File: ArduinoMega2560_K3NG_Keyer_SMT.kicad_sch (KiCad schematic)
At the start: 44 parts, among them J10 Conn_01x05_Strip, J11 Conn_01x05_Strip, J12 Conn_01x05_Strip, J13 Conn_01x05_Strip, J2 Conn_01x02, J23 Conn_01x02, J25 Conn_01x05_Strip, J26 Conn_01x05_Strip, J27 Conn_01x05_Strip, J28 Conn_01x05_Strip, J29 Conn_01x05_Strip, J30 Conn_01x05_Strip, J31 Conn_01x05_Strip, J32 Conn_01x05_Strip, J33 Conn_01x05_Strip, J34 Conn_01x05_Strip, J35 Conn_01x05_Strip, J36 Conn_01x05_Strip, J37 Conn_01x05_Strip, J38 Conn_01x05_Strip, J39 Conn_01x05_Strip, J40 Conn_01x05_Strip, J41 Conn_01x05_Strip, J42 Conn_01x05_Strip, J43 Conn_01x05_Strip, J44 Conn_01x05_Strip, J45 Conn_01x05_Strip, J46 Conn_01x05_Strip, J47 Conn_01x05_Strip, J48 Conn_01x05_Strip, J49 Conn_01x05_Strip, J50 Conn_01x05_Strip, J51 Conn_01x05_Strip, J52 Conn_01x05_Strip, J53 Conn_01x05_Strip, J54 Conn_01x05_Strip, J56 Conn_01x05_Strip, J6 Conn_01x05_Strip, J7 Conn_01x05_Strip, J8 Conn_01x05_Strip, J9 Conn_01x05_Strip

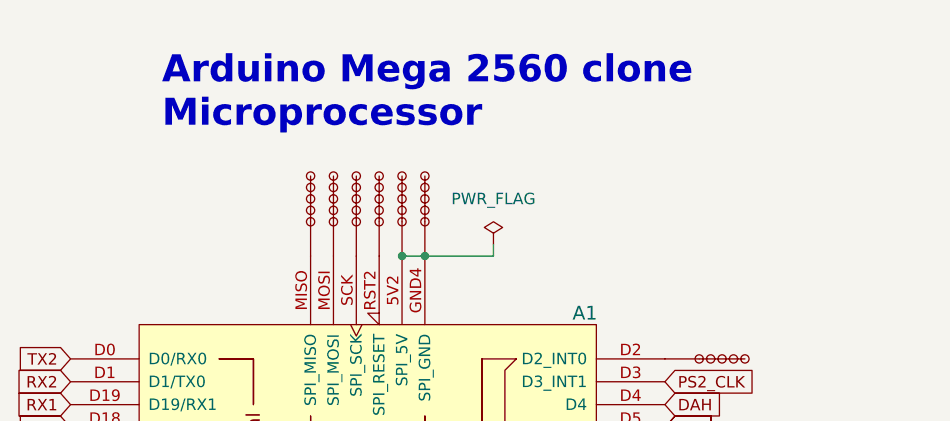
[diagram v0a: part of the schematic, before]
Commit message: First attempt at locating parts on PCB. Also, many changes to footprints.
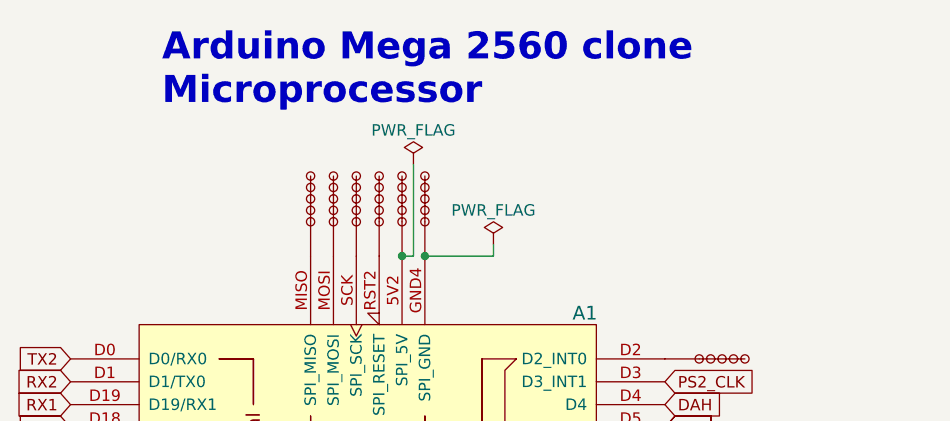
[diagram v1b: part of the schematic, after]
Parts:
- removed J56: Conn_01x05_Strip, User:01x05_Strip, symbol User_KICAD6:Conn_01x05_Strip
- added J15: Conn_01x05_Strip, User:01x05_Strip, symbol User_KICAD6:Conn_01x05_Strip
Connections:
- net at A1.A12: now also J29.1 (Pin_1); no longer J30. (Pin_1)
- net at A1.D34: now also J42.1 (Pin_1); no longer J42. (Pin_1)
- net at A1.A8: now also J25.1 (Pin_1); no longer J26. (Pin_1)
- net at A1.D36: now also J41.1 (Pin_1); no longer J41. (Pin_1)
- net at A1.A4: now also J11.1 (Pin_1); no longer J11. (Pin_1)
- net at A1.A11: now also J28.1 (Pin_1); no longer J29. (Pin_1)
- net at A1.D30: now also J43.1 (Pin_1); no longer J43. (Pin_1)
- net at A1.A7: now also J15.1 (Pin_1); no longer J25. (Pin_1)
- net at A1.D47: now also J37.1 (Pin_1); no longer J37. (Pin_1)
- net at A1.RST2 (SPI_RESET): now also J52.1 (Pin_1); no longer J51. (Pin_1)
- net at A1.A10: now also J26.1 (Pin_1); no longer J28. (Pin_1)
- net at A1.MOSI (SPI_MOSI): now also J50.1 (Pin_1); no longer J53. (Pin_1)
- net at A1.MISO (SPI_MISO): now also J49.1 (Pin_1); no longer J54. (Pin_1)
- net at A1.A6: now also J13.1 (Pin_1); no longer J13. (Pin_1)
- net at A1.A9: now also J27.1 (Pin_1); no longer J27. (Pin_1)
- net at A1.3V31 (3.3V): now also J34.1 (Pin_1); no longer J35. (Pin_1)
- net at A1.3V32 (3.3V): now also J35.1 (Pin_1); no longer J36. (Pin_1)
- net at A1.A13: now also J30.1 (Pin_1); no longer J31. (Pin_1)
- net at A1.A14: now also J31.1 (Pin_1); no longer J32. (Pin_1)
- net at A1.A15: now also J32.1 (Pin_1); no longer J33. (Pin_1)
- net at A1.A2: now also J10.1 (Pin_1); no longer J10. (Pin_1)
- net at A1.A5: now also J12.1 (Pin_1); no longer J12. (Pin_1)
- net at A1.AREF: now also J33.1 (Pin_1); no longer J34. (Pin_1)
- net at A1.D14 (D14/TX3): now also J9.1 (Pin_1); no longer J9. (Pin_1)
- net at A1.D15 (D15/RX3): now also J8.1 (Pin_1); no longer J8. (Pin_1)
- net at A1.D16 (D16/TX2): now also J7.1 (Pin_1); no longer J7. (Pin_1)
- net at A1.D17 (D17/RX2): now also J6.1 (Pin_1); no longer J6. (Pin_1)
- net at A1.D2 (D2_INT0): now also J48.1 (Pin_1); no longer J48. (Pin_1)
- net at A1.D22: now also J47.1 (Pin_1); no longer J47. (Pin_1)
- net at A1.D24: now also J46.1 (Pin_1); no longer J46. (Pin_1)
- net at A1.D26: now also J45.1 (Pin_1); no longer J45. (Pin_1)
- net at A1.D28: now also J44.1 (Pin_1); no longer J44. (Pin_1)
- net at A1.D44: now also J40.1 (Pin_1); no longer J40. (Pin_1)
- net at A1.D45: now also J39.1 (Pin_1); no longer J39. (Pin_1)
- net at A1.D46: now also J38.1 (Pin_1); no longer J38. (Pin_1)
- net at A1.D53 (D53_CS): now also J36.1 (Pin_1)
- net at A1.SCK (SPI_SCK): now also J51.1 (Pin_1); no longer J52. (Pin_1)
- new net: A1.5V2 (SPI_5V), J53.1 (Pin_1)
- new net: A1.GND4 (SPI_GND), J54.1 (Pin_1)
